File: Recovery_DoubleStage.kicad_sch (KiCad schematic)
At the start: 0 parts

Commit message: forgot to add project and schematic changes
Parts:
- added C6: 2.2nF 50V, symbol Device:C
- added C7: 0.1microF 4v, symbol Device:C
- added C8: 0.1microF 2V, symbol Device:C
- added C?: 10nF, symbol Device:C
- added IC?: TXB0108PWR, SOP65P640X120-20N, symbol TXB0108PWR:TXB0108PWR
- added IC?: MPU-6050, MPU6050, symbol MPU-6050:MPU-6050
- added R? (x2): 10k, symbol Device:R
- added U?: RFM95W-868S2, XCVR_RFM95W-868S2, symbol RFM95W-868S2:RFM95W-868S2
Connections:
- new net: C8.1, IC?.10 (REGOUT)
- new net: C6.2, IC?.20 (CPOUT)
- new net +3V3: C7.2, C?.1, IC?.13 (VDD), IC?.2 (VCCA), IC?.8 (VLOGIC), R?.1, R?.2, U?.13 (3_3V)
- new net +5V: IC?.19 (VCCB)
- new net GND: C6.1, C7.1, C8.2, C?.2, IC?.11 (GND), IC?.18 (GND), U?.1 (GND), U?.10 (GND@2), U?.8 (GND@1)
- new net LoRa_RESET: IC?.6 (A5), U?.6 (RESET)
- new net LoRa_RESET_5V: IC?.15 (B5)
- new net LoRa_SS: IC?.5 (A4), U?.5 (NSS)
- new net LoRa_SS_5V: IC?.16 (B4)
- new net MISO: IC?.1 (A1), U?.2 (MISO)
- new net MISO_5V: IC?.20 (B1)
- new net MOSI: IC?.3 (A2), U?.3 (MOSI)
- new net MOSI_5V: IC?.18 (B2)
- new net SCK: IC?.4 (A3), U?.4 (SCK)
- new net SCK_5V: IC?.17 (B3)
- new net SCL: IC?.13 (B7)
- new net SCL_3V3: IC?.7 (A6), IC?.8 (A7), R?.1, R?.2
- new net SDA: IC?.14 (B6)
- no-connect marks 0 -> 13
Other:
- added sheet microcontroller (microcontroller.kicad_sch)
- note added: "All MPU-6050 caps are ceramic, X7R, +-10% tolerance"
- note added: "OE should be kept low until VCCB and VCCA are ready"

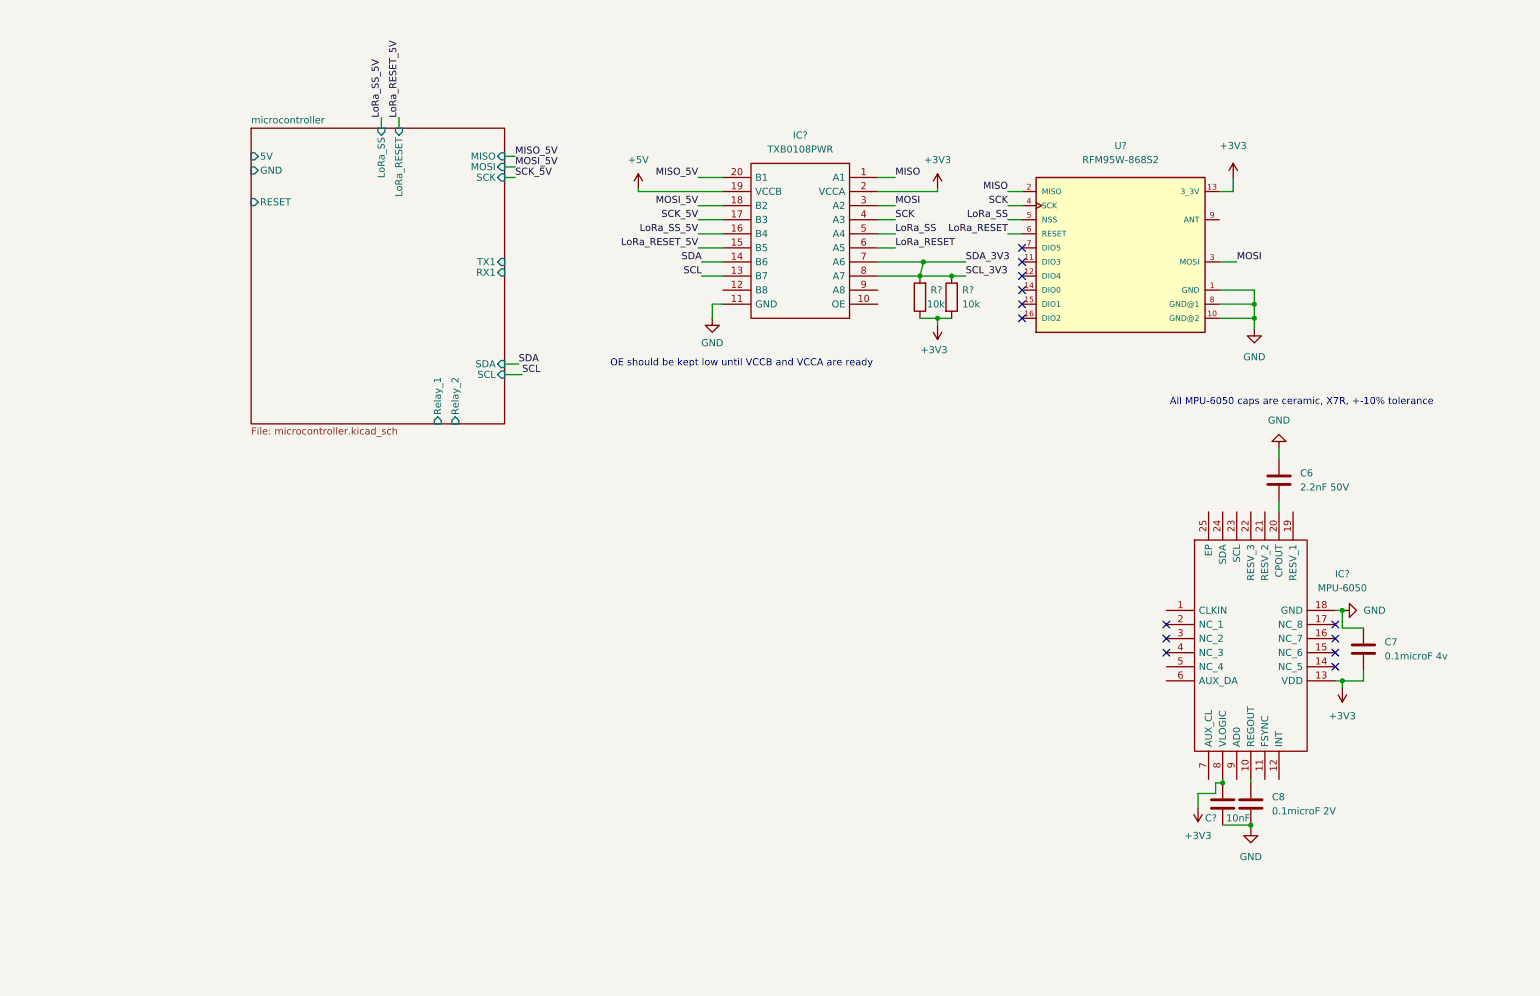
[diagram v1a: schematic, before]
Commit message: atmega2560 at 3v3 now. almost done with  SD card
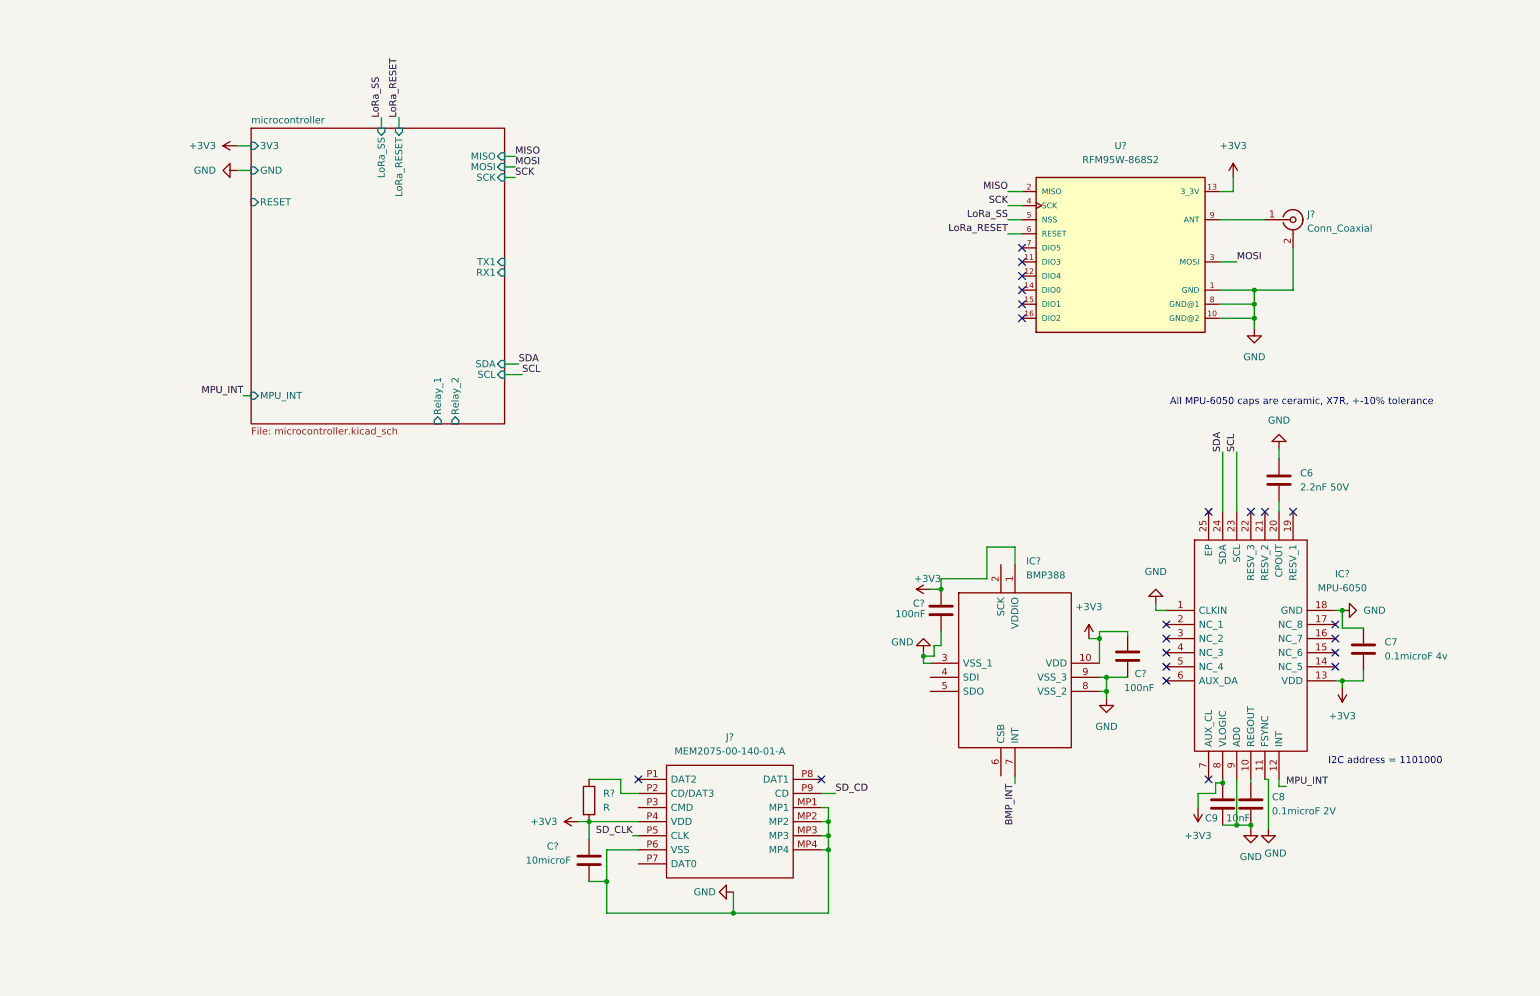
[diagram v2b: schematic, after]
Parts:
- removed IC?: TXB0108PWR, SOP65P640X120-20N, symbol TXB0108PWR:TXB0108PWR
- removed R? (x2): 10k, symbol Device:R
- added C? (x2): 100nF, symbol Device:C
- added C?: 10microF, symbol Device:C
- added IC?: BMP388, BMP388, symbol BMP388:BMP388
- added J?: Conn_Coaxial, symbol Connector:Conn_Coaxial
- added J?: MEM2075-00-140-01-A, MEM20750014001A, symbol MEM2075-00-140-01-A:MEM2075-00-140-01-A
- added R?: R, symbol Device:R
- gave numbers to parts that had none: 1
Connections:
- net +3V3: now also C?.1, C?.1, C?.1, IC?.1 (VDDIO), IC?.10 (VDD), J?.P4 (VDD), R?.2
- net GND: now also IC?.1 (CLKIN), IC?.11 (FSYNC), IC?.9 (AD0), C?.2, C?.2, C?.2, IC?.3 (VSS_1), IC?.8 (VSS_2), IC?.9 (VSS_3), J?.2 (Ext), J?.MP1, J?.MP2, J?.MP3, J?.MP4, J?.P6 (VSS)
- net SCL: now also IC?.23 (SCL)
- net SDA: now also IC?.24 (SDA)
- net MPU_INT: now reaches IC?.12 (INT)
- net at U?.9 (ANT): now also J?.1 (In)
- new net: J?.P2 (CD/DAT3), R?.1
- new net BMP_INT: IC?.7 (INT)
- new net SD_CD: J?.P9 (CD)
- new net SD_CLK: J?.P5 (CLK)
- no-connect marks 13 -> 22
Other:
- sheet microcontroller ports: added 3V3, MPU_INT; removed 5V
- note added: "I2C address = 1101000"
- note removed: "OE should be kept low until VCCB and VCCA are ready"

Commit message: did power rails,  gps, and SD card, and altimiter.
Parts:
- added BZ?: Buzzer, symbol Device:Buzzer
- added C? (x4): 10u, symbol Device:C
- added C? (x2): 0.1u, symbol Device:C
- added C? (x2): 47n, symbol Device:C
- added IC?: AP2210N-3.3TRG1, SOT95P280X145-3N, symbol AP2210N-3.3TRG1:AP2210N-3.3TRG1
- added IC?: NEO-6M-0, NEO6M0, symbol NEO-6M-0:NEO-6M-0
- added J?: Conn_Coaxial, symbol Connector:Conn_Coaxial
- added K1, K2: ALQ105, ALQ105, symbol ALQ105:ALQ105
- added L?: 27nH, symbol Device:L
- added Q? (x2): BSS138, Package_TO_SOT_SMD:SOT-23, symbol Transistor_FET:BSS138
- added R?: 100k, symbol Device:R
- added R? (x2): 1M, symbol Device:R
- added U?: NCP5501DT50RKG, symbol custom:NCP5501DT50RKG
- C6: value 2.2nF 50V -> 2.2n
- C7: value 0.1microF 4v -> 0.1u
- C8: value 0.1microF 2V -> 0.1u
- C9: value 10nF -> 10n
- C? (x2): value 100nF -> 100n
- C?: value 10microF -> 10u
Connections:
- net +3V3: now also IC?.6 (CSB), C?.1, C?.1, C?.2, C?.2, IC?.23 (VCC), L?.1, R?.2
- net GND: now also IC?.5 (SDO), C?.2, C?.2, IC?.10 (GND_1), IC?.12 (GND_2), IC?.13 (GND_3), IC?.22 (V_BCKP), IC?.24 (GND_4), IC?.7 (VDDUSB), J?.2 (Ext), Q?.2 (S), Q?.2 (S), R?.1, R?.1
- net LoRa_RESET: now also R?.1
- net MISO: now also J?.P7 (DAT0)
- net MOSI: now also J?.P3 (CMD)
- net SCL: now also IC?.2 (SCK)
- net SDA: now also IC?.4 (SDI)
- new net: C?.1, C?.1, C?.2, C?.2, IC?.1 (GND), U?. (VOUT)
- new net: K2.5 (COIL_2), Q?.3 (D)
- new net: K1.5 (COIL_2), Q?.3 (D)
- new net: IC?.11 (RF_IN), J?.1 (In), L?.2
- new net: C?.1, C?.1
- new net: IC?.8 (RESERVED_2), IC?.9 (VCC_RF)
- new net 3V3: C?.2, IC?.2 (VOUT)
- new net 5V: C?.2, U?. (VOUT)
- new net RX1: IC?.20 (TXD1)
- new net Relay_1: Q?.1 (G), R?.2
- new net Relay_2: Q?.1 (G), R?.2
- new net TX1: IC?.21 (RXD1)
- new net VBAT: C?.1, C?.1, IC?.3 (VIN), U?. (VOUT)
- no-connect marks 22 -> 36

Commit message: updating schematic
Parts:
- removed K2: ALQ105, ALQ105, symbol ALQ105:ALQ105
- removed Q? (x2): BSS138, Package_TO_SOT_SMD:SOT-23, symbol Transistor_FET:BSS138
- removed R?: 1M, symbol Device:R
- added D? (x3): D, symbol Device:D
- added J? (x2): Screw_Terminal_01x02, symbol Connector:Screw_Terminal_01x02
- added K?: ALQ105, ALQ105, symbol ALQ105:ALQ105
- added Q? (x3): BSS138, Package_TO_SOT_SMD:SOT-23, symbol Transistor_FET:BSS138
- added R? (x3): 100, symbol Device:R
- added R? (x2): 10k, symbol Device:R
- BZ?: value Buzzer -> TE054003-5
- C10, C11: renamed from C?; value 100n -> 0.1u
- R?: value 1M -> 10k
- R?: value R -> 10k
- gave numbers to parts that had none: 2
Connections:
- net GND is gone; now on net -BATT: C10.2, C11.2, C12.2, C13.2, C6.1, C7.1, C8.2, C9.2, C?.2, IC?.1 (CLKIN), IC?.10 (GND_1), IC?.11 (FSYNC), IC?.12 (GND_2), IC?.13 (GND_3), IC?.18 (GND), IC?.22 (V_BCKP), IC?.24 (GND_4), IC?.3 (VSS_1), IC?.5 (SDO), IC?.7 (VDDUSB), IC?.8 (VSS_2), IC?.9 (AD0), IC?.9 (VSS_3), J?.2 (Ext), J?.2 (Ext), J?.MP1 (SHIELD), J?.MP2 (SHIELD), J?.MP3 (SHIELD), J?.MP4 (SHIELD), J?.P6 (VSS), R?.1, U?.1 (GND), U?.10 (GND@2), U?.8 (GND@1)
- net Relay_1: now also R?.1; no longer R?.2
- net Relay_2: now also R?.1
- net -BATT: now reaches C?.1, C?.1, C?.2, C?.2, IC?.1 (GND), U?. (VOUT)
- net -BATT: now also J?.1 (Pin_1), J?.1 (Pin_1), Q?.2 (S), Q?.2 (S), Q?.2 (S), R?.1, R?.1
- net at K1.5 (COIL_2): now also Q?.3 (D)
- net +5V: now reaches K1.1 (COIL_1)
- net +5V: now also BZ?.1 (-), D?.1 (K), D?.1 (K), D?.1 (K), K?.1 (COIL_1)
- net Igniter_Detection_1: now reaches K1.2 (NC)
- net +BATT: now reaches K1.3 (NO)
- net +BATT: now also C?.1, C?.1, IC?.3 (VIN), U?. (VOUT), K?.3 (NO)
- net at K1.4 (COM): now also J?.2 (Pin_2)
- net at BZ?.2 (+): now also D?.2 (A), Q?.3 (D)
- net LoRa_SS renamed LoRa_CS
- net SD_CD renamed SD_CS
- removed net VBAT: C?.1, C?.1, IC?.3 (VIN), U?. (VOUT)
- new net: Q?.1 (G), R?.2, R?.2 (x3)
- new net: J?.2 (Pin_2), K?.4 (COM)
- new net: K?.5 (COIL_2), Q?.3 (D)
- new net Buzzer: R?.1
- new net Igniter_Detection_2: K?.2 (NC)
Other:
- sheet microcontroller ports: added BMP_INT, Buzzer, ID1, ID2, LoRa_CS, SD_CS; removed LoRa_SS
- note added: "Coil resistance 62.5 ohm @ 80 mA Gate voltage: 3.26 v Drain resistor dissipation 1 mW"
- note added: "Pin current draw 40 mA"
- moved on the sheet: BZ?

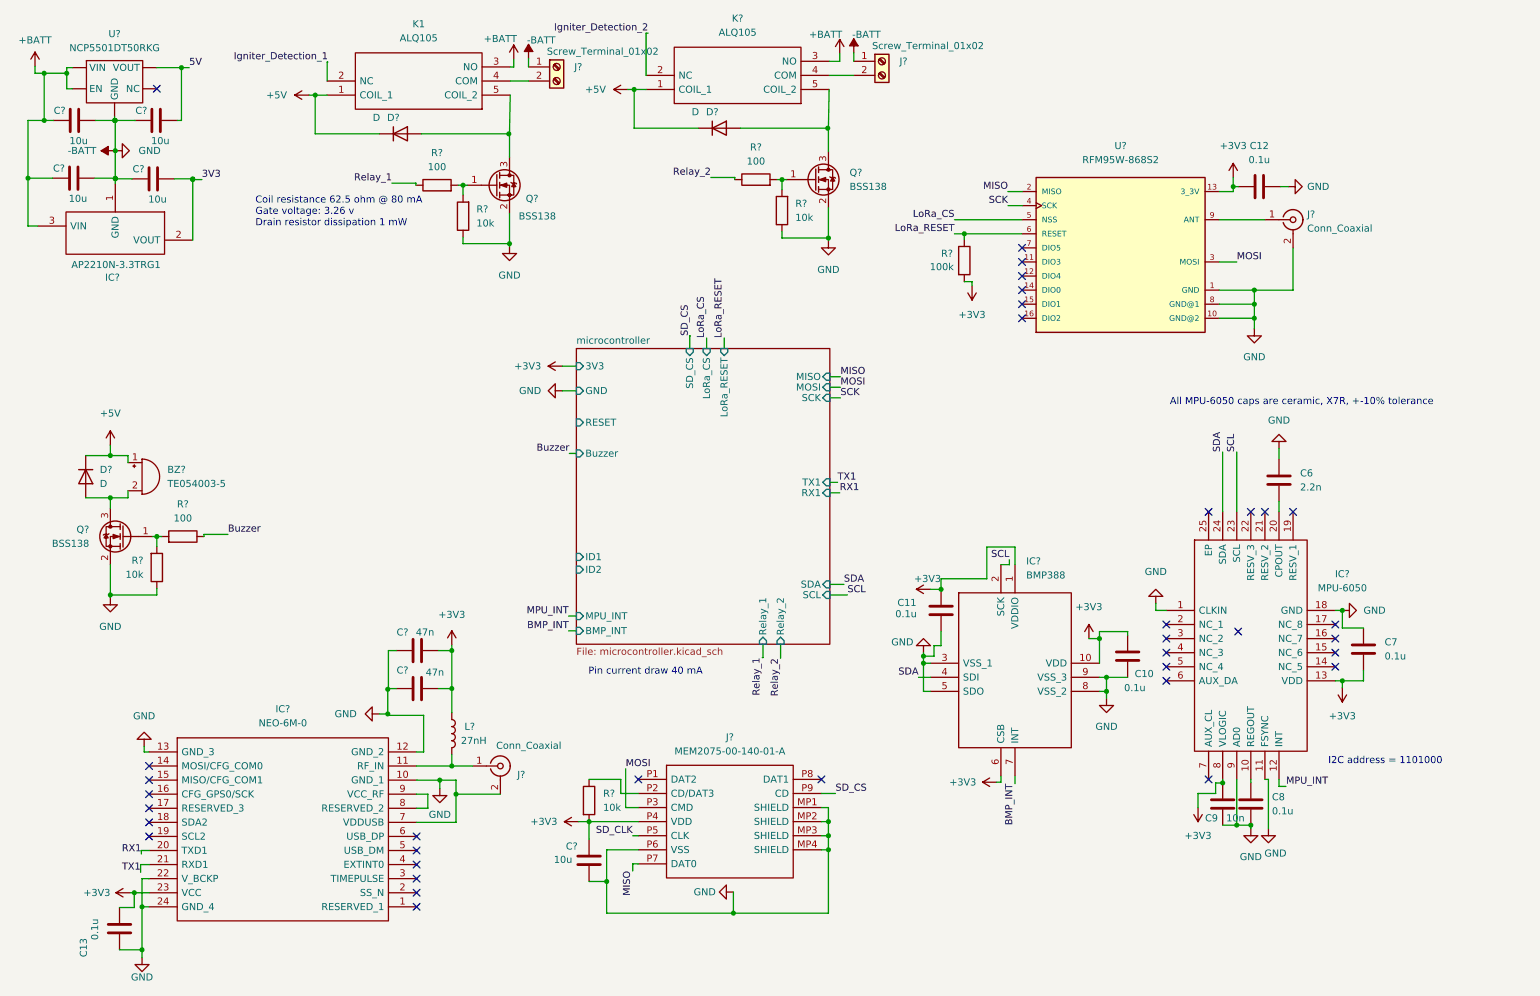
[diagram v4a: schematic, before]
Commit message: added ignition detection circuit
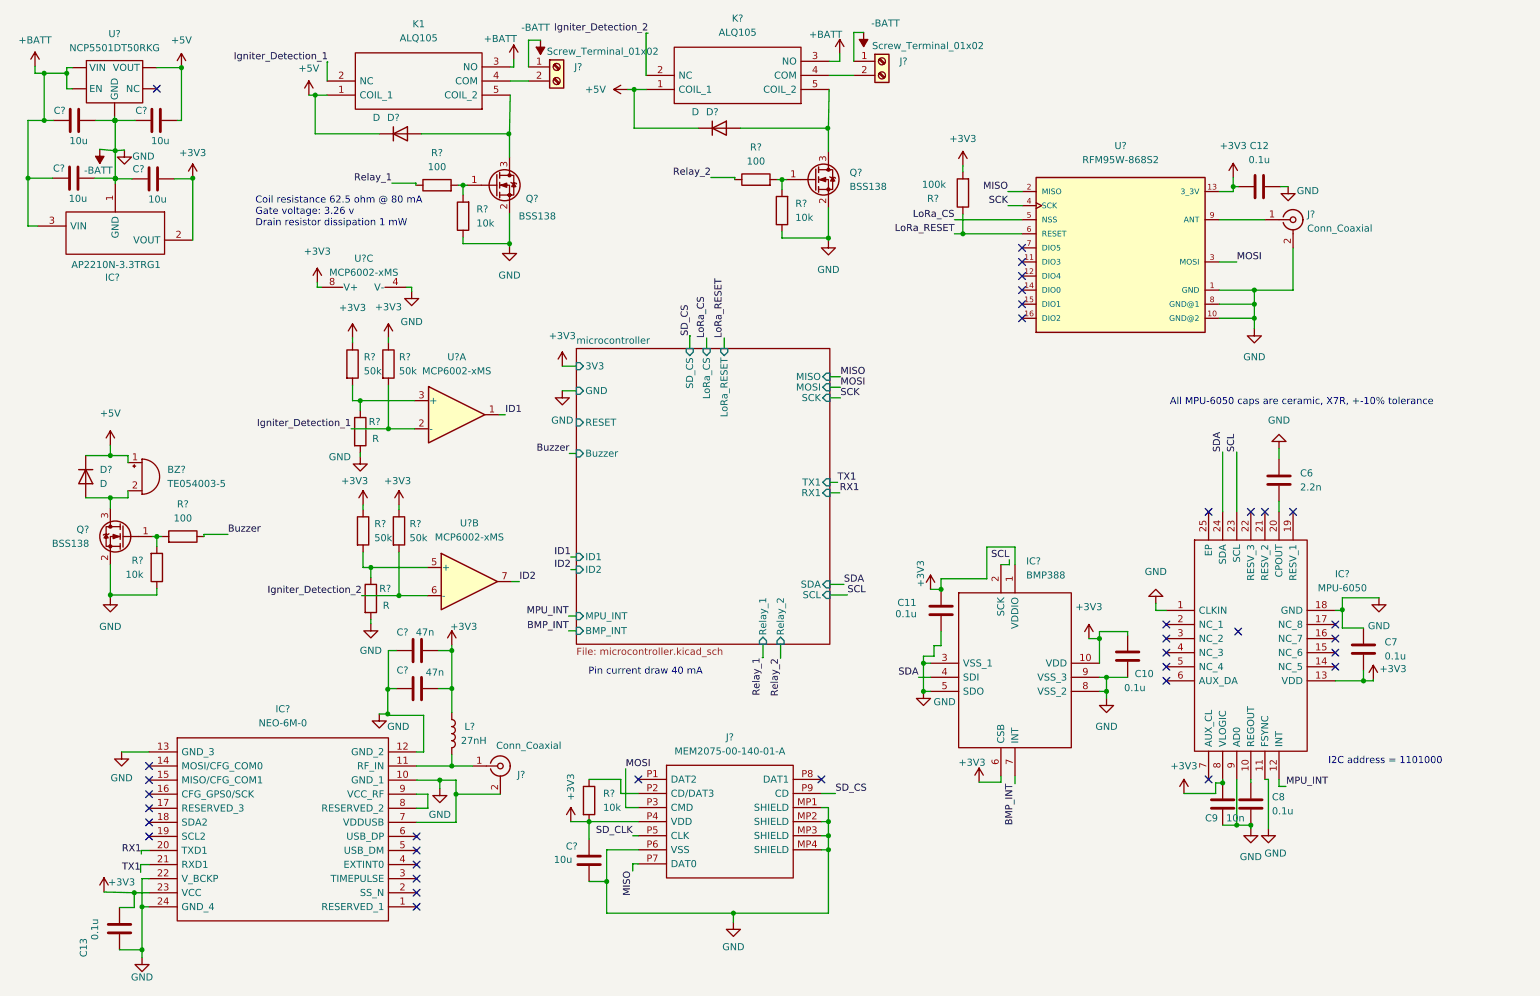
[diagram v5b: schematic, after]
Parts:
- added R? (x4): 50k, symbol Device:R
- added R? (x2): R, symbol Device:R
- added U? (x3): MCP6002-xMS, symbol Amplifier_Operational:MCP6002-xMS
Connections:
- net +3V3: now also R?.1, R?.1, R?.1, R?.1, U?.8 (V+)
- net +5V: now also C?.2, U?. (VOUT)
- net -BATT: now also R?.2, R?.2, U?.4 (V-); no longer C7.1, IC?.18 (GND)
- net Igniter_Detection_1: now also R?.2, U?.2 (-)
- net Igniter_Detection_2: now also R?.2, U?.6 (-)
- net 3V3: no longer names the net of C?.2, IC?.2 (VOUT)
- removed net 5V: C?.2, U?. (VOUT)
- new net: R?.1, R?.2, U?.3 (+)
- new net: C7.1, IC?.18 (GND)
- new net: R?.1, R?.2, U?.5 (+)
- new net ID1: U?.1
- new net ID2: U?.7
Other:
- moved on the sheet: R?
